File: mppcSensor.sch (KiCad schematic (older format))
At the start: 2 parts, among them J1 Conn_Coaxial

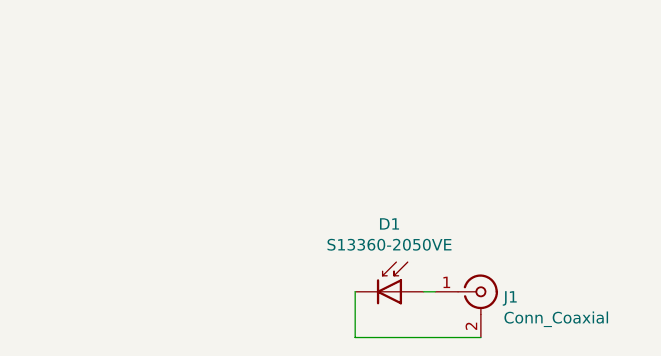
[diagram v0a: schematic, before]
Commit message: Changed to kicad, sensor only boards
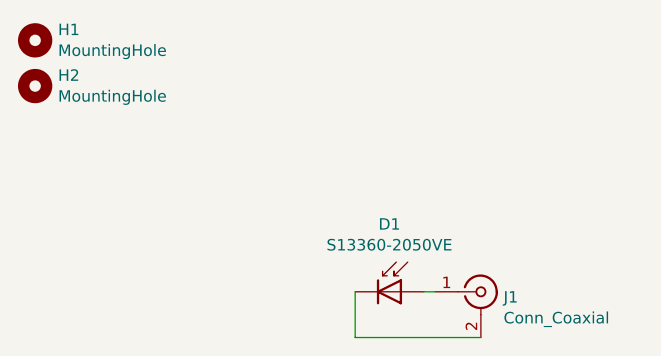
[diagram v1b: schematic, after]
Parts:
- added H1, H2: MountingHole, MountingHole:MountingHole_2.2mm_M2_ISO14580_Pad, symbol Mechanical:MountingHole
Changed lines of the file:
@@
 EESchema Schematic File Version 4
+LIBS:mppcSensor-cache
 EELAYER 26 0
 EELAYER END
@@
 Wire Wire Line
 	2200 2100 2200 1900
+$Comp
+L Mechanical:MountingHole H1
+U 1 1 5C710CBA
+P 800 800
+F 0 "H1" H 900 846 50  0000 L CNN
+F 1 "MountingHole" H 900 755 50  0000 L CNN
+F 2 "MountingHole:MountingHole_2.2mm_M2_ISO14580_Pad" H 800 800 50  0001 C CNN
+F 3 "~" H 800 800 50  0001 C CNN
+	1    800  800
+	1    0    0    -1
+$EndComp
+$Comp
+L Mechanical:MountingHole H2
+U 1 1 5C710D04
+P 800 1000
+F 0 "H2" H 900 1046 50  0000 L CNN
+F 1 "MountingHole" H 900 955 50  0000 L CNN
+F 2 "MountingHole:MountingHole_2.2mm_M2_ISO14580_Pad" H 800 1000 50  0001 C CNN
+F 3 "~" H 800 1000 50  0001 C CNN
+	1    800  1000
+	1    0    0    -1
+$EndComp
 $EndSCHEMATC
